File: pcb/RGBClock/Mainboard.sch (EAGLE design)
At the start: 93 parts, among them IC1 MCP23017SO, K1 G6K-2F, K2 G6K-2F, K3 G6K-2F, K4 G6K-2F, Q1 32.768KHz, Q2 32.768KHz, U1 MAX6369KA+T, U10 NX3L1G384GW, U11 NX3L1G384GW, U12 DRV612PW, U13 2N7002-7-F, U14 2N7002-7-F, U15 2N7002-7-F, U16 2N7002-7-F, U17 TPS71533DCKR, U2 TXS0102DCUR, U3 P82B96DR, U4 LM2675M-5.0, U5 DS1338Z-33+, U6 SI4735-D50, U7 TPS71533DCKR, U8 NX3L1G384GW, U9 NX3L1G384GW, X2 43045-0400, X3 1503_09, X4 1503_09, X5 43045-0800

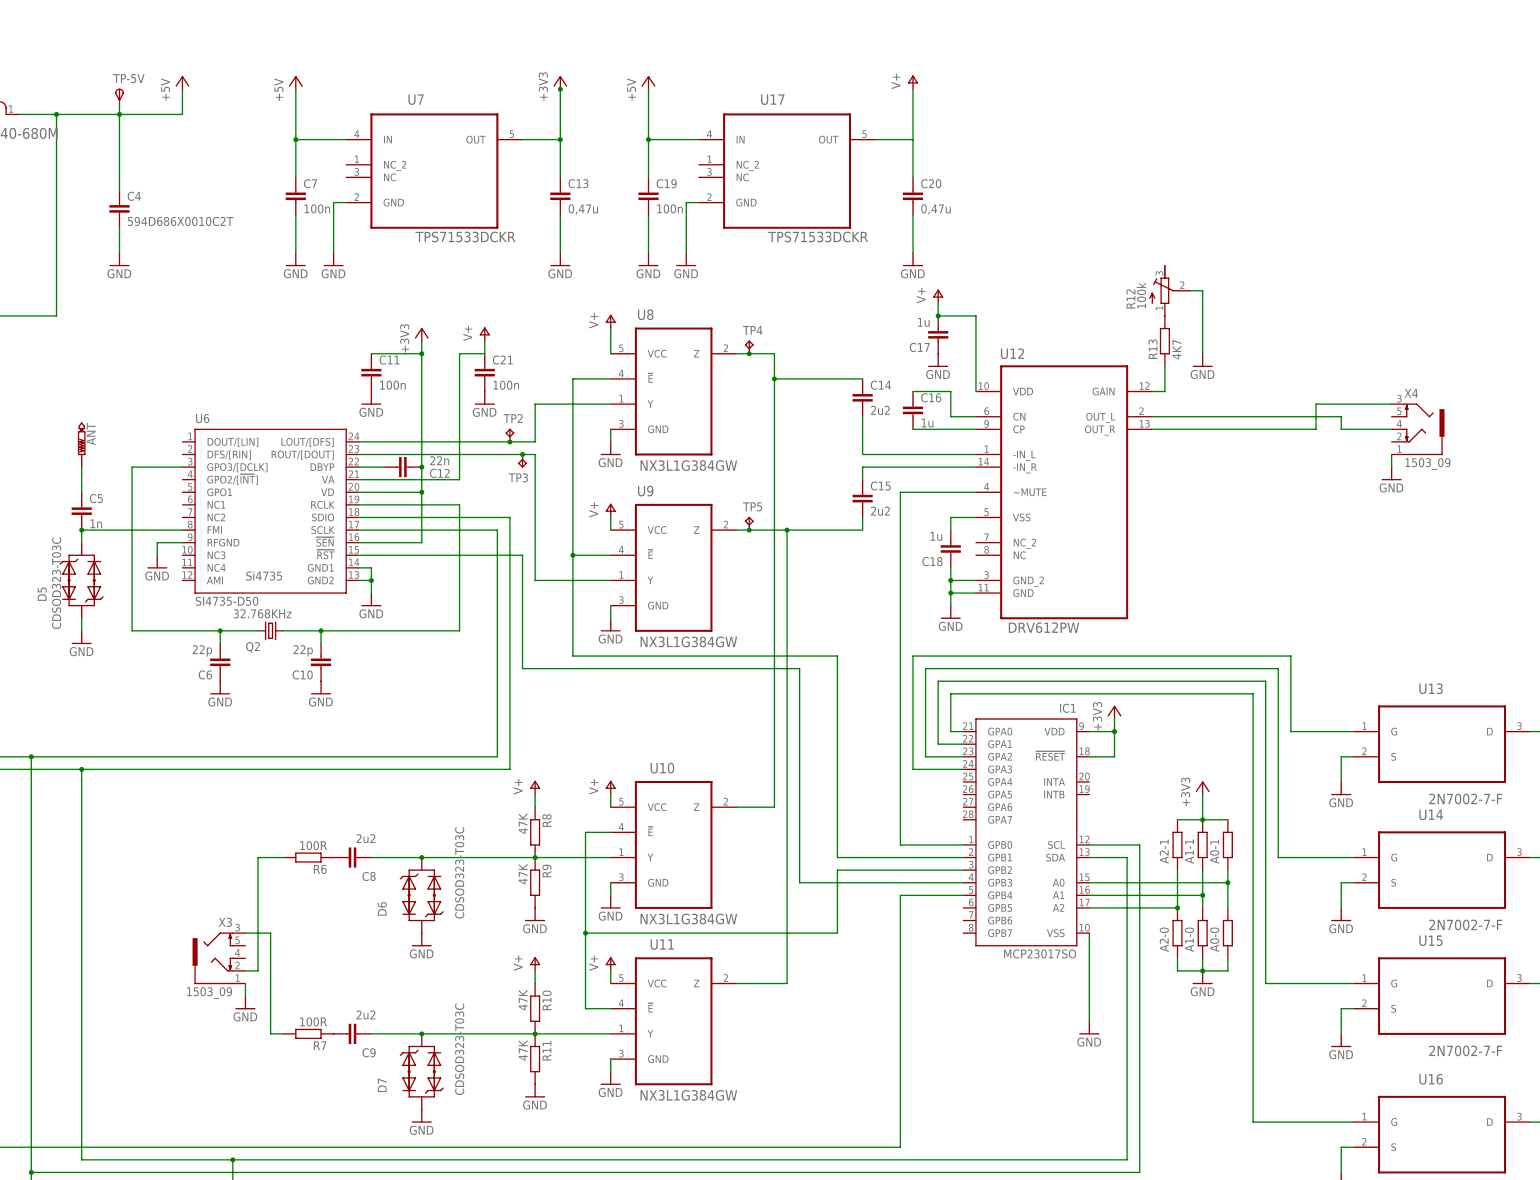
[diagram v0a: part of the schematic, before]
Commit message: updating component packages
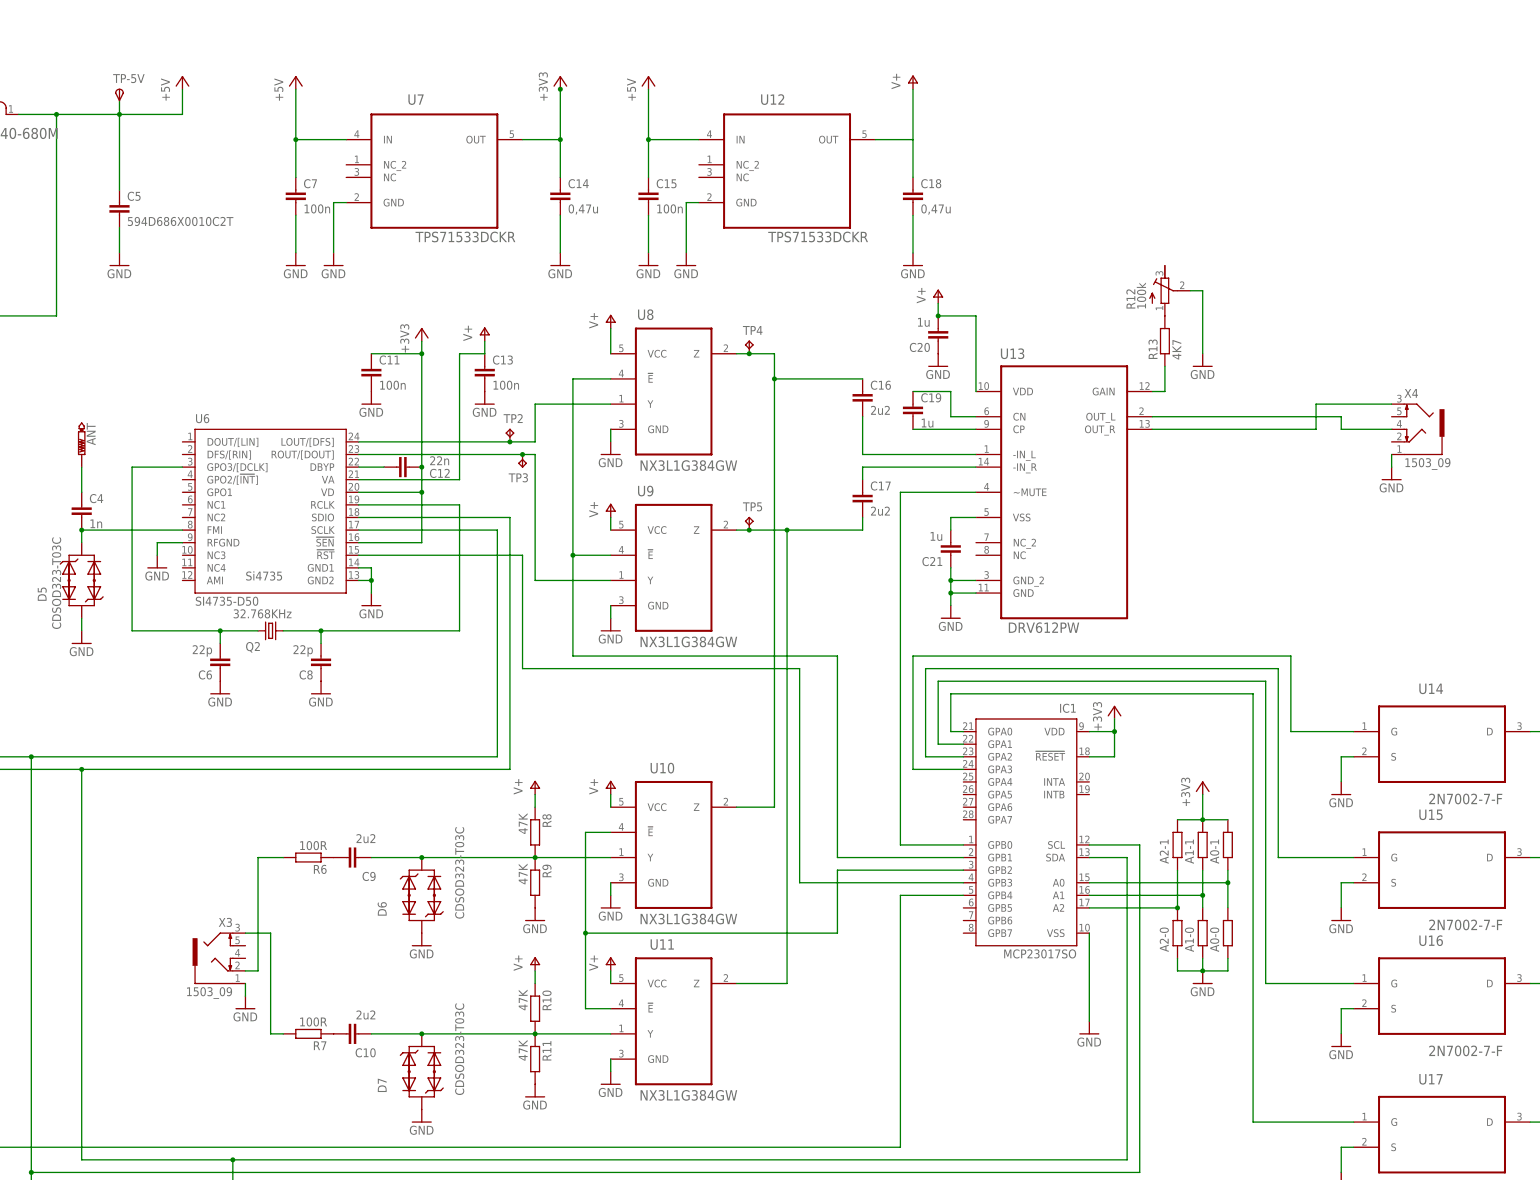
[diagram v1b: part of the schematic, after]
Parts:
- C10: value 22p -> 2u2
- C11, C12: device rcl:C-EUC1005 -> rcl:C-EUC0805
- C13: value 0,47u -> 100n; device rcl:C-EUC1206 -> rcl:C-EUC0805
- C14: value 2u2 -> 0,47u; device rcl:C-EUC1005 -> rcl:C-EUC0805
- C15: value 2u2 -> 100n; device rcl:C-EUC1005 -> rcl:C-EUC0805
- C16, C17: value 1u -> 2u2
- C18: value 1u -> 0,47u; device rcl:C-EUC1005 -> rcl:C-EUC0805
- C19: value 100n -> 1u; device rcl:C-EUC0805 -> rcl:C-EUC1005
- C20: value 0,47u -> 1u; device rcl:C-EUC1206 -> rcl:C-EUC1005
- C21: value 100n -> 1u
- C4: value 594D686X0010C2T -> 1n; device MyComponents:594D686X0010C2T -> rcl:C-EUC0402
- C5: value 1n -> 594D686X0010C2T; device rcl:C-EUC1005 -> MyComponents:594D686X0010C2T
- C6: device rcl:C-EUC1005 -> rcl:C-EUC0402
- C8: value 2u2 -> 22p; device rcl:C-EUC1005 -> rcl:C-EUC0402
- U12: value DRV612PW -> TPS71533DCKR; device Texas:DRV612PW -> Texas:TPS71533DCKR
- U13: value 2N7002-7-F -> DRV612PW; device Diodes:2N7002-7-F -> Texas:DRV612PW
- U17: value TPS71533DCKR -> 2N7002-7-F; device Texas:TPS71533DCKR -> Diodes:2N7002-7-F
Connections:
- net +3V3: now also C14.1; no longer C13.1
- net +5V: now also C15.1, C5.1, U12.IN; no longer C19.1, C4.1, U17.IN
- net 3V3A: now also C13.1, C18.1, C20.2, U12.OUT, U13.VDD; no longer C17.2, C20.1, C21.1, U12.VDD, U17.OUT
- net GND: now also C14.2, C15.2, C18.2, C20.1, C21.1, C5.2, C8.1, U13.GND, U13.GND_2, U17.S; no longer C10.1, C17.1, C18.1, C19.2, C20.2, C21.2, C4.2, U12.GND_2, U13.S, U17.GND
- net N$18: now also U14.G; no longer U13.G
- net N$19: now also U15.G; no longer U14.G
- net N$21: now also U16.G; no longer U15.G
- net N$22: now also U14.D; no longer U13.D
- net N$23: now also U15.D; no longer U14.D
- net N$24: now also U16.D; no longer U15.D
- net N$29: now also C16.1; no longer C14.1
- net N$30: now also C17.2; no longer C15.2
- net N$32: now also C8.2; no longer C10.2
- net N$36: now also C10.2; no longer C9.2
- net N$37: now also C9.2; no longer C8.2
- net N$38: now also U13.~MUTE; no longer U12.~MUTE
- net N$40: now also U13.OUT_L; no longer U12.OUT_L
- net N$44: now also U13.OUT_R; no longer U12.OUT_R
- net N$46: now also U13.GAIN; no longer U12.GAIN
- net N$48: now also C9.1; no longer C8.1
- net N$50: now also C10.1; no longer C9.1
- net N$53: now also C16.2, U13.-IN_L; no longer C14.2, U12.-IN_L
- net N$54: now also C19.2, U13.CP; no longer C16.2, U12.CP
- net N$55: now also C17.1, U13.-IN_R; no longer C15.1, U12.-IN_R
- net N$56: now also C19.1, U13.CN; no longer C16.1, U12.CN
- net N$57: now also C21.2, U13.VSS; no longer C18.2, U12.VSS
- net N$58: now also C4.1; no longer C5.1
- net N$59: now also C4.2; no longer C5.2
- net N$7: now also U17.G; no longer U16.G
- net N$9: now also U17.D; no longer U16.D
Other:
- moved on the sheet: C10, C13, C14, C15, C16, C17, C18, C19, C20, C21, C8, C9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

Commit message: Main and Display updated
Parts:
- removed G1: CR2032H, battery:CR2032H
- added B1: HU2032-LF, MyComponents:HU2032-LF
- C10, C16, C17, C9: device rcl:C-EUC1005 -> rcl:C-EUC0805
- R1: value 160 -> 3K48
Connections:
- net GND: now also B1.-; no longer G1.-
- net N$16: now also B1.+; no longer G1.+
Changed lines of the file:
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@@
 <part name="U3" library="Texas" deviceset="P82B96DR" device=""/>
 <part name="GND13" library="supply1" deviceset="GND" device=""/>
-<part name="R1" library="rcl" deviceset="R-EU_" device="0204/7" value="160"/>
+<part name="R1" library="rcl" deviceset="R-EU_" device="0204/7" value="3K48"/>
 <part name="LED1" library="led" deviceset="LED" device="5MM" value="5mm Led"/>
 <part name="GND25" library="supply1" deviceset="GND" device=""/>
@@
 <part name="+3V3" library="supply1" deviceset="+3V3" device=""/>
 <part name="U13" library="Texas" deviceset="DRV612PW" device=""/>
-<part name="G1" library="battery" deviceset="CR2032H" device=""/>
 <part name="U5" library="Maxim_By_element14_Batch_1" deviceset="DS1338Z-33+" device=""/>
 <part name="U14" library="Diodes" deviceset="2N7002-7-F" device=""/>
@@
 <part name="R11" library="resistor" deviceset="R-EU_" device="0204/2V" value="47K"/>
 <part name="GND38" library="supply1" deviceset="GND" device=""/>
-<part name="C9" library="rcl" deviceset="C-EU" device="C1005" value="2u2"/>
-<part name="C10" library="rcl" deviceset="C-EU" device="C1005" value="2u2"/>
-<part name="C16" library="rcl" deviceset="C-EU" device="C1005" value="2u2"/>
-<part name="C17" library="rcl" deviceset="C-EU" device="C1005" value="2u2"/>
+<part name="C9" library="rcl" deviceset="C-EU" device="C0805" value="2u2"/>
+<part name="C10" library="rcl" deviceset="C-EU" device="C0805" value="2u2"/>
+<part name="C16" library="rcl" deviceset="C-EU" device="C0805" value="2u2"/>
+<part name="C17" library="rcl" deviceset="C-EU" device="C0805" value="2u2"/>
 <part name="C19" library="rcl" deviceset="C-EU" device="C1005" value="1u"/>
 <part name="GND39" library="supply1" deviceset="GND" device=""/>
@@
 <part name="P+14" library="supply1" deviceset="V+" device=""/>
 <part name="P+16" library="supply1" deviceset="V+" device=""/>
+<part name="B1" library="MyComponents" deviceset="HU2032-LF" device=""/>
 </parts>
 <sheets>
@@
 <attribute name="VALUE" x="275.6154" y="50.3936" size="2.0828" layer="96" ratio="10" rot="SR0"/>
 </instance>
-<instance part="G1" gate="1" x="63.5" y="-99.06" rot="R90"/>
 <instance part="U5" gate="A" x="99.06" y="-83.82"/>
 <instance part="U14" gate="A" x="363.22" y="30.48"/>
@@
 <instance part="P+14" gate="1" x="180.34" y="20.32"/>
 <instance part="P+16" gate="1" x="180.34" y="-15.24"/>
+<instance part="B1" gate="G$1" x="63.5" y="-99.06" rot="R90"/>
 </instances>
 <busses>
@@
 <wire x1="78.74" y1="-96.52" x2="78.74" y2="-106.68" width="0.1524" layer="91"/>
 <wire x1="78.74" y1="-106.68" x2="71.12" y2="-106.68" width="0.1524" layer="91"/>
-<pinref part="G1" gate="1" pin="-"/>
 <wire x1="71.12" y1="-106.68" x2="63.5" y2="-106.68" width="0.1524" layer="91"/>
 <wire x1="63.5" y1="-106.68" x2="63.5" y2="-104.14" width="0.1524" layer="91"/>
@@
 <wire x1="71.12" y1="-106.68" x2="71.12" y2="-114.3" width="0.1524" layer="91"/>
 <junction x="71.12" y="-106.68"/>
+<pinref part="B1" gate="G$1" pin="-"/>
 </segment>
 <segment>
@@
 <segment>
 <pinref part="U5" gate="A" pin="VBAT"/>
-<pinref part="G1" gate="1" pin="+"/>
 <wire x1="81.28" y1="-81.28" x2="63.5" y2="-81.28" width="0.1524" layer="91"/>
 <wire x1="63.5" y1="-81.28" x2="63.5" y2="-93.98" width="0.1524" layer="91"/>
-</segment>
-</net>
+<pinref part="B1" gate="G$1" pin="+"/>
+</segment>
+</net>

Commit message: alle componenten naar mainboard.lbr
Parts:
- removed ANT: PTR1PAD1-13, testpad:PTR1PAD1-13
- removed C15: 100n, rcl:C-EUC0805
- removed C18: 0,47u, rcl:C-EUC0805
- removed D5: CDSOD323-T03C, MyComponents:CDSOD323-T03C
- removed U12: TPS71533DCKR, Texas:TPS71533DCKR
- removed U6: SI4735-D50, SiliconLabs:SI4735-D50
- removed X1: (no value), con-berg:PN87520
- added C22, C23, C27, C28: 1u, Mainboard:RCL_C-EUC0805
- added C24, C25, C26, C29: 8.2p, Mainboard:RCL_C-EUC0805
- added IC2: LT1763CS8-1.5, Mainboard:LINEAR-TECHNOLOGY_LT1763CS8-1.5
- added JP2: (no value), Mainboard:JUMPER_JP1E
- added R20: A0-1, Mainboard:RESISTOR_R-EU_R0402:1
- added R21: A0-0, Mainboard:RESISTOR_R-EU_R0402:1
- added R22: A1-1, Mainboard:RESISTOR_R-EU_R0402:1
- added R24: A1-0, Mainboard:RESISTOR_R-EU_R0402:1
- added U$1: 18nH, Mainboard:MAINBOARD_L-0603
- added U$2: MAINBOARD_SI4684-A10-GMQF, Mainboard:MAINBOARD_SI4684-A10-GMQF
- added U$3: CGA0603MLC-05E, Mainboard:MAINBOARD_CGA0603MLC-05E
- added U$4: 120nH, Mainboard:MAINBOARD_L-0603
- added U$5: 22nH, Mainboard:MAINBOARD_L-0603
- added X6: ST-SMB-H, Mainboard:MAINBOARD_ST-SMB-H
- B1: device MyComponents:HU2032-LF -> Mainboard:MYCOMPONENTS_HU2032-LF
- C1, C10, C14, C16, C17, C3, C7, C9: device rcl:C-EUC0805 -> Mainboard:RCL_C-EUC0805
- C11: value 100n -> 8.2p; device rcl:C-EUC0805 -> Mainboard:RCL_C-EUC0805
- C12: value 22n -> 8.2p; device rcl:C-EUC0805 -> Mainboard:RCL_C-EUC0805
- C13: value 100n -> 1u; device rcl:C-EUC0805 -> Mainboard:RCL_C-EUC0805
- C19, C20, C21: device rcl:C-EUC1005 -> Mainboard:RCL_C-EUC1005
- C2: device rcl:C-EUC1206 -> Mainboard:RCL_C-EUC1206
- C4: value 1n -> 10n; device rcl:C-EUC0402 -> Mainboard:RCL_C-EUC0805
- C5: device MyComponents:594D686X0010C2T -> Mainboard:MYCOMPONENTS_594D686X0010C2T
- C6: value 22p -> 100n; device rcl:C-EUC0402 -> Mainboard:RCL_C-EUC0805
- C8: value 22p -> 33p; device rcl:C-EUC0402 -> Mainboard:RCL_C-EUC0805
- CON1: device con-harting:CON26 -> Mainboard:CON-HARTING_CON26
- D1: device diode:MUR150RL -> Mainboard:DIODE_MUR150RL
- D10, D11, D8, D9: device diode:1N4148DO35-7 -> Mainboard:DIODE_1N4148DO35-7
- D2, D3: device MyComponents:SMA6F -> Mainboard:MYCOMPONENTS_SMA6F
- D4: device diode:DIODE-DO-214AC -> Mainboard:DIODE_DIODE-DO-214AC
- D6, D7: device MyComponents:CDSOD323-T03C -> Mainboard:MYCOMPONENTS_CDSOD323-T03C
- IC1: device Microchip:MCP23017SO -> Mainboard:MICROCHIP_MCP23017SO
- JP1: device jumper:JP1E -> Mainboard:JUMPER_JP1E
- K1, K2, K3, K4: device relay:G6K-2F -> Mainboard:RELAY_G6K-2F
- L1: device Bourns_By_element14_Batch_1:SRR1240-680M -> Mainboard:BOURNS_BY_ELEMENT14_BATCH_1_SRR1240-680M
- LED1: device led:LED5MM -> Mainboard:LED_LED5MM
- Q1: device crystal:CRYSTALTC26V -> Mainboard:CRYSTAL_CRYSTALTC26V
- Q2: value 32.768KHz -> (none); device crystal:CRYSTALTC26V -> Mainboard:MAINBOARD_CRYSTAL_CRYSTALSM49
- R1: device rcl:R-EU_0204/7 -> Mainboard:RCL_R-EU_M1206
- R10, R11, R13, R6, R7, R8, R9: device resistor:R-EU_0204/2V -> Mainboard:RCL_R-EU_M1206
- R12: device resistor:R-TRIMM4G/J -> Mainboard:RESISTOR_R-TRIMM4G/J
- R14, R15, R16, R17, R18, R19: device resistor:R-EU_R0402 -> Mainboard:RESISTOR_R-EU_R0402:1
- R2, R3: device resistor:R-EU_0204/5 -> Mainboard:RCL_R-EU_M1206
- R4, R5: value 680R -> 275R; device resistor:R-EU_0204/2V -> Mainboard:RCL_R-EU_M1206
- TP-5V: value TPSTP10SQ -> TESTPAD_TPSTP10SQ; device testpad:TPSTP10SQ -> Mainboard:TESTPAD_TPSTP10SQ
- TP2, TP3, TP4, TP5, TP6, TP7: value TPTP07SQ -> TESTPAD_TPTP07SQ; device testpad:TPTP07SQ -> Mainboard:TESTPAD_TPTP07SQ
- U1: device Maxim_By_element14_Batch_1:MAX6369KA+T -> Mainboard:MAXIM_BY_ELEMENT14_BATCH_1_MAX6369KA+T
- U10, U11, U8, U9: device NXP_By_element14_Batch_1:NX3L1G384GW -> Mainboard:NXP_BY_ELEMENT14_BATCH_1_NX3L1G384GW
- U13: device Texas:DRV612PW -> Mainboard:TEXAS_DRV612PW
- U14, U15, U16, U17: device Diodes:2N7002-7-F -> Mainboard:DIODES_2N7002-7-F
- U2: device Texas:TXS0102DCUR -> Mainboard:TEXAS_TXS0102DCUR
- U3: device Texas:P82B96DR -> Mainboard:TEXAS_P82B96DR
- U4: device Texas:LM2675M-5.0 -> Mainboard:TEXAS_LM2675M-5.0
- U5: device Maxim_By_element14_Batch_1:DS1338Z-33+ -> Mainboard:MAXIM_BY_ELEMENT14_BATCH_1_DS1338Z-33+
- U7: device Texas:TPS71533DCKR -> Mainboard:TEXAS_TPS71533DCKR
- X2: device con-molex-micro-fit-3_0:HEADER_POS4_43045-0401 -> Mainboard:CON-MOLEX-MICRO-FIT-3_0_HEADER_POS4_43045-0401
- X3, X4: value 1503_09 -> CON-LUMBERG_1503_09; device con-lumberg:1503_09 -> Mainboard:CON-LUMBERG_1503_09
- X5: device con-molex-micro-fit-3_0:HEADER_POS8_43045-0800 -> Mainboard:CON-MOLEX-MICRO-FIT-3_0_HEADER_POS8_43045-0800
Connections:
- removed net 3V3A: C13.1, C18.1, C20.2, R10.1, R8.1, U10.VCC, U11.VCC, U12.OUT, U13.VDD, U6.VA, U8.VCC, U9.VCC
- removed net N$62: IC1.SCL, TP6.TP, U5.SCL, U6.SCLK
- new net +1.8V: C4.1, IC2.OUT, IC2.SENSE
- new net +24V: C11.1, C12.1, C13.1, C22.1, C28.2, C29.2, U$2.VA, U$2.VCORE, U$2.VMEM
- new net N$26: Q2.2, U$2.XTALO
- new net N$34: C24.2, TP2.TP, U$2.ROUT, U9.Y
- new net N$68: C12.2, C22.2, U$2.ABYP
- new net N$69: C23.2, U$2.DACREF
- new net N$70: C11.2, C13.2, C26.2, C27.2, C28.1, C29.1, U$2.DBYP
- new net SCL: IC1.SCL, R3.1, TP6.TP, U$2.SCLK, U2.B2, U3.SY, U5.SCL
- new net SDA: IC1.SDA, R2.1, TP7.TP, U$2.MOSI, U2.B1, U3.SX, U5.SDA
- net +3V3: now also C20.2, C26.1, C27.1, R10.1, R20.2, R22.2, R8.1, U$2.SMODE, U$2.VIO, U10.VCC, U11.VCC, U13.VDD, U8.VCC, U9.VCC; no longer C11.1, C12.1, U6.!SEN, U6.VD
- net +5V: now also C6.1, IC2.!SHDN, IC2.IN, JP2.2; no longer C15.1, U12.IN, X1.1
- net GND: now also C23.1, C24.1, C25.1, C6.2, IC2.GND@1, IC2.GND@2, IC2.GND@3, R21.1, R24.1, U$2.GNDD1, U$2.GNDD2, U$2.GNDD3, U$2.GNDD4, U$2.RFREF1, U$2.RFREF2, U$2.RFREF3, U$2.RFREF4, U$3.1, U$4.1, X6.2; no longer C11.2, C13.2, C15.2, C18.2, C6.1, C8.1, D5.P$1, U12.GND, U6.GND1, U6.GND2, U6.RFGND, X1.4
- net N$14: now also R20.1, R21.2, U$2.MISO; no longer R2.1, U2.B1, U3.SX
- net N$2: now also U$2.XTALI; no longer C6.2, U6.GPO3/[DCLK]
- net N$27: now also C25.2, TP3.TP, U$2.LOUT; no longer TP2.TP, U6.LOUT/[DFS]
- net N$28: now also C8.1, U$3.2, X6.1; no longer TP3.TP, U6.ROUT/[DOUT], U9.Y
- net N$32: now also U$2.VHFSW, U$5.1; no longer C8.2, Q2.2, U6.RCLK
- net N$35: now also U$2.!RSTB; no longer U6.!RST
- net N$4: now also CON1.2, JP2.1; no longer IC1.SDA, TP7.TP, U5.SDA, U6.SDIO
- net N$40: now also X4.2
- net N$44: now also X4.5
- net N$47: now also X3.4
- net N$49: now also X3.5
- net N$58: now also C4.2, IC2.BYP; no longer ANT.TP, C4.1
- net N$59: now also U$1.2, U$2.VHFI, U$4.2, U$5.2; no longer C4.2, D5.P$2, U6.FMI
- net N$61: now also C8.2, U$1.1; no longer C12.2, U6.DBYP
- net N$65: now also R22.1, R24.2, U$2.SSB; no longer R3.1, U2.B2, U3.SY
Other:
- moved on the sheet: B1, C10, C11, C12, C13, C4, C6, C8, C9, CON1, D2, D3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

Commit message: all components on board
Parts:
- R1, R10, R11, R13, R2, R3, R4, R5, R6, R7, R8, R9: device Mainboard:RCL_R-EU_M1206 -> rcl:R-EU_M0805
- U$2: value MAINBOARD_SI4684-A10-GMQF -> SI4684-A10
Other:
- moved on the sheet: C4, C6, IC2
